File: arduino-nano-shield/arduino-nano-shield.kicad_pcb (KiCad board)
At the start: 2 copper layers, 36.5 x 64 mm, 16 parts, among them J1 ELRS, J2 M1, J3 M2, J4 LED_D11, J5 LED_D11, J6 SPWR, J7 I2C, J8 SERVO, Q1 BD139, Q2 2N3904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

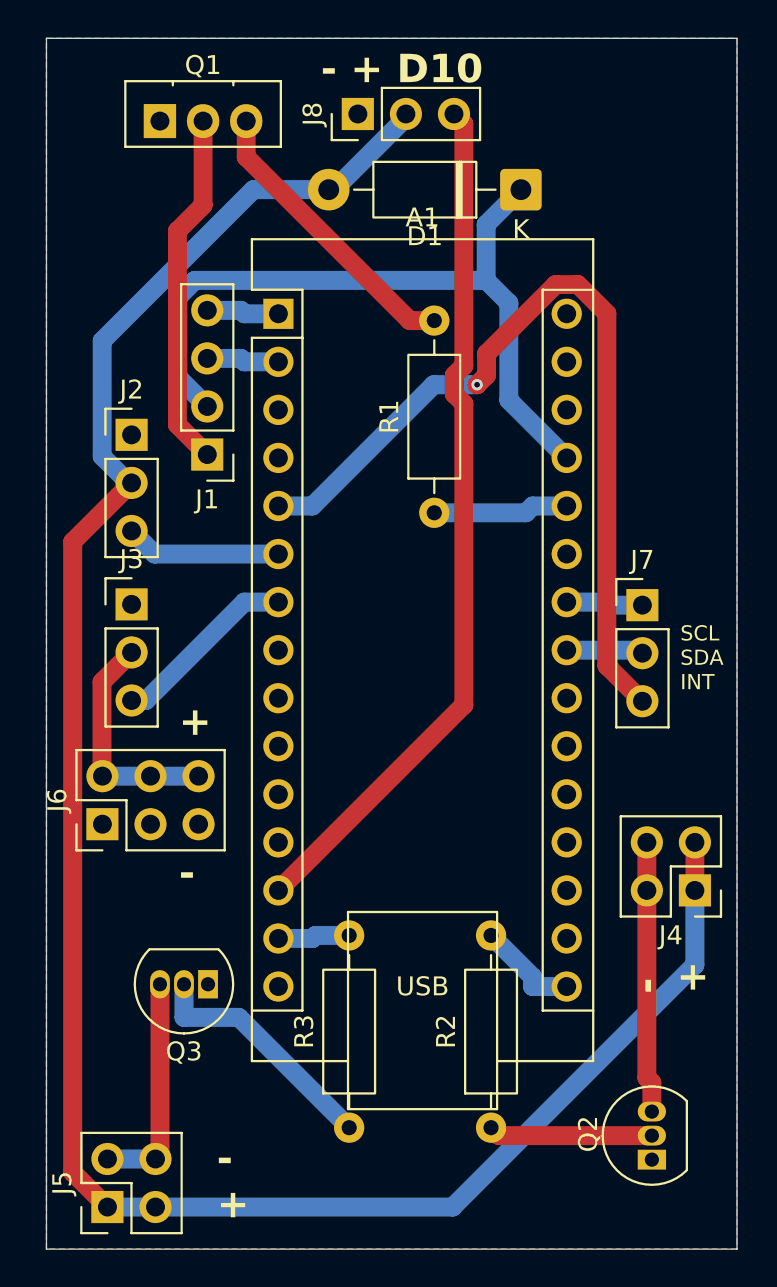
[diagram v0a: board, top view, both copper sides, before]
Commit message: Add V2 board
- jumper for powering second ESC header VCC from main VCC net
- GPS header with D5/D6
- support two servos on servo header
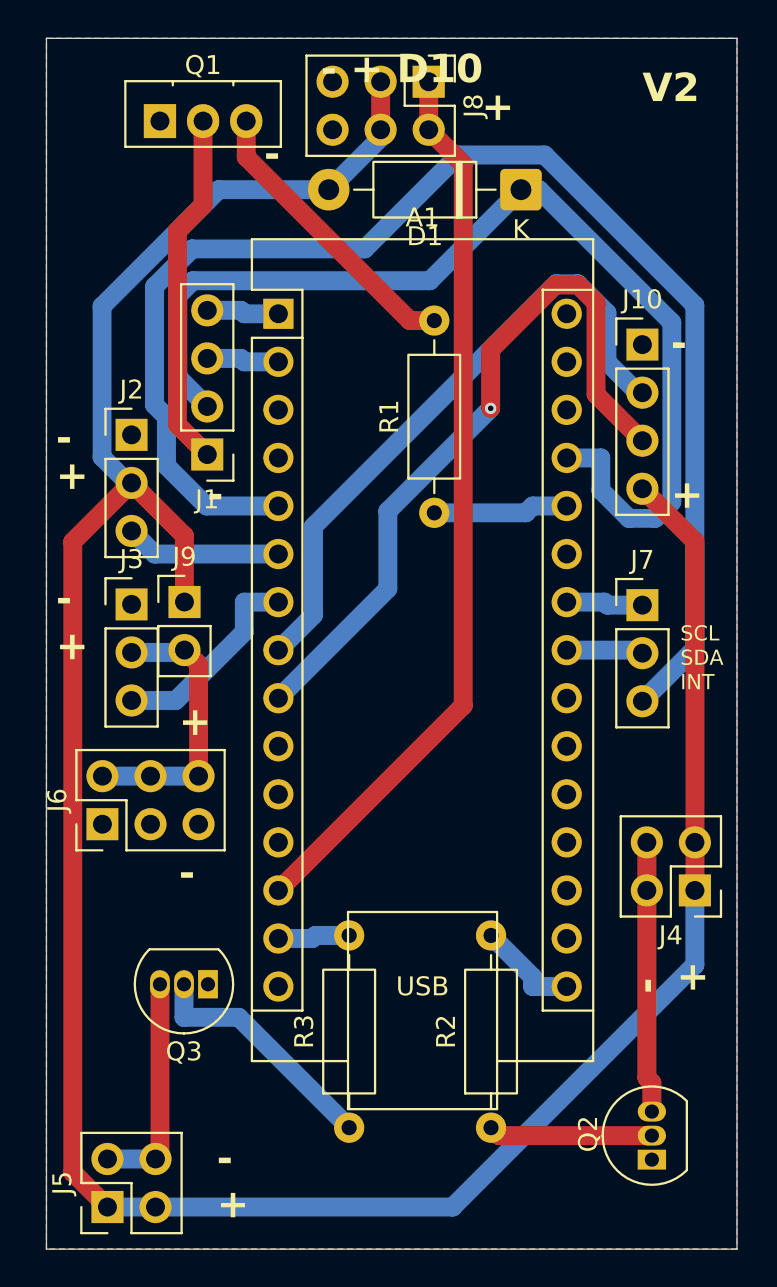
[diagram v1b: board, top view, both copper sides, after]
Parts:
- added J10: ELRS, Connector_PinHeader_2.54mm:PinHeader_1x04_P2.54mm_Vertical, F.Cu at (114.0, 69.7)
- added J9: JP1, Connector_PinHeader_2.54mm:PinHeader_1x02_P2.54mm_Vertical, F.Cu at (89.8, 83.3)
- J8: footprint Connector_PinHeader_2.54mm:PinHeader_1x03_P2.54mm_Vertical -> Connector_PinHeader_2.54mm:PinHeader_2x03_P2.54mm_Vertical
- moved J8 4.11 mm to (102.7, 55.8), turned to -90 degrees
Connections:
- A1 pad 8: unconnected-(A1-D5-Pad8) -> /GTX_D5
- A1 pad 9: unconnected-(A1-D6-Pad9) -> /GRX_D6
- J8 pad 1: GND -> /D10
- J8 pad 2: VCC -> /D10
- J8 pad 3: /D10 -> VCC
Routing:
- net /GRX_D6: track 0.00 -> 38.7 mm, vias 0 -> 1
- net /GTX_D5: track 0.00 -> 33.9 mm
- net VCC: track 112.5 -> 141.9 mm
- net /INT: track 44.8 -> 73.3 mm, vias 1 -> 0
- net Net-(A1-+5V): track 39.8 -> 55.6 mm
- net Net-(J3-Pin_2): track 12.3 -> 14.9 mm
- net /D10: track 45.7 -> 47.5 mm
- net Net-(A1-D4): track 9.91 -> 10.8 mm
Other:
- board text added: "V2"

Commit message: Add v2.1 board
- add three pin header as alternative for LED connections (populate
  with angled header) to connect to various multiplexing controllers
- add headers for A20 and A21 as aux connectors
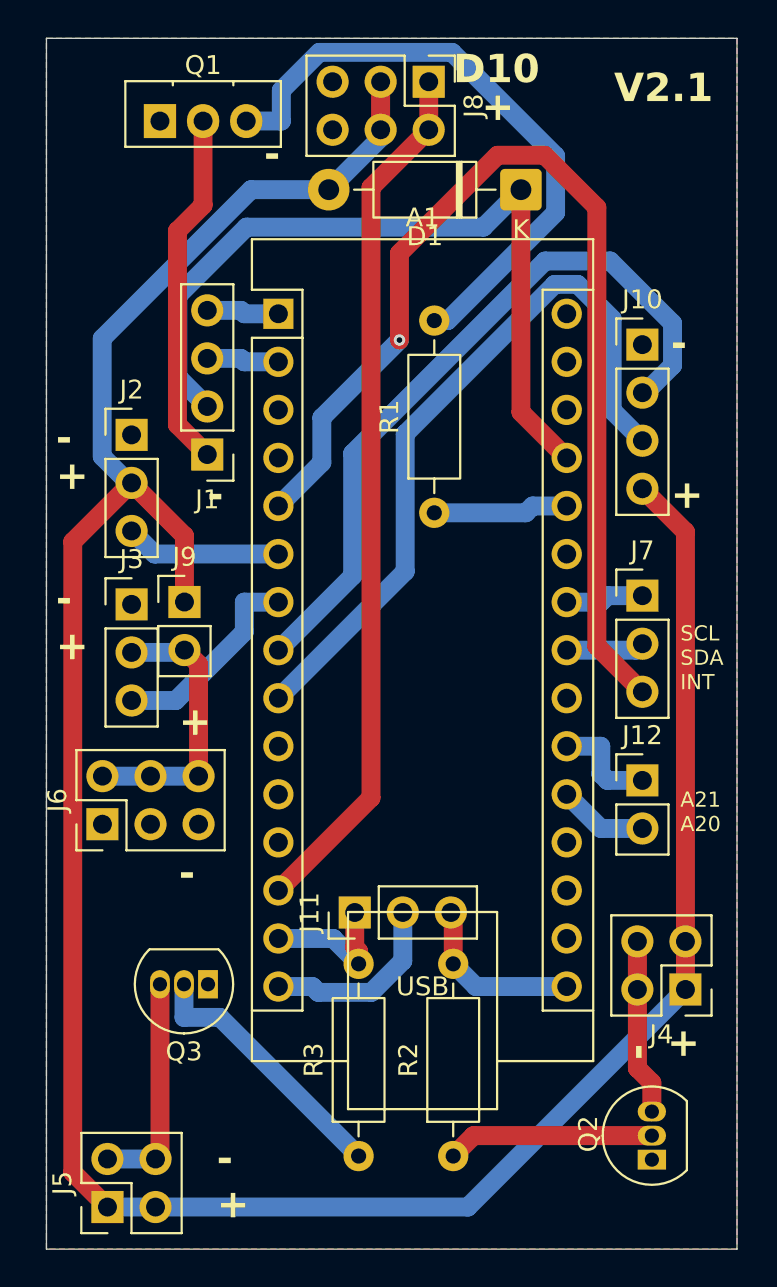
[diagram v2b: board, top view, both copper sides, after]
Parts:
- added J11: LED, Connector_PinHeader_2.54mm:PinHeader_1x03_P2.54mm_Vertical, F.Cu at (98.8, 99.7)
- added J12: AUX, Connector_PinHeader_2.54mm:PinHeader_1x02_P2.54mm_Vertical, F.Cu at (114.0, 92.7)
- J10: value ELRS -> GPS
- moved J4 5.26 mm to (116.3, 103.8)
- moved R2 2.50 mm to (104.0, 112.6)
- moved R3 1.58 mm to (99.0, 112.6)
- moved J7 0.50 mm to (114.0, 83.0)
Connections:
- A1 pad 15: unconnected-(A1-MISO-Pad15) -> Net-(A1-MISO)
- A1 pad 20: unconnected-(A1-A1-Pad20) -> Net-(A1-A1)
- A1 pad 21: unconnected-(A1-A2-Pad21) -> Net-(A1-A2)
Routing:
- net Net-(Q1-B): track 15.4 -> 32.8 mm
- net /INT: track 73.3 -> 56.3 mm, vias 0 -> 1
- net Net-(A1-+5V): track 55.6 -> 42.1 mm
- net Net-(A1-MISO): track 0.00 -> 9.95 mm
- net Net-(A1-A2): track 0.00 -> 5.60 mm
- net Net-(J4-Pin_2): track 14.3 -> 9.31 mm
- net /GTX_D5: track 33.9 -> 38.9 mm
- net Net-(A1-A1): track 0.00 -> 4.75 mm
- net Net-(A1-SCK): track 5.41 -> 9.26 mm
- net Net-(A1-MOSI): track 3.81 -> 7.59 mm
- net Net-(Q2-B): track 8.67 -> 10.9 mm
- net /D10: track 47.5 -> 46.0 mm
- net Net-(Q3-B): track 12.9 -> 14.0 mm
- net VCC: track 141.9 -> 140.9 mm
- net /GRX_D6: track 38.7 -> 38.8 mm, vias 1 -> 0
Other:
- board text added: "A21 A20"
- board text added: "D10"
- board text added: "V2.1"
- board text removed: "- + D10"
- board text removed: "V2"
